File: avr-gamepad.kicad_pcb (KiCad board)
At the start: 2 copper layers, 26.7 x 48.3 mm, 33 parts, among them J1 Conn_01x08, J2 Conn_01x01, P1 USB_C_Plug_USB2.0, SW10 Up, SW11 Down, SW12 Left, SW13 Select, SW2 R, SW3 X, SW4 A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

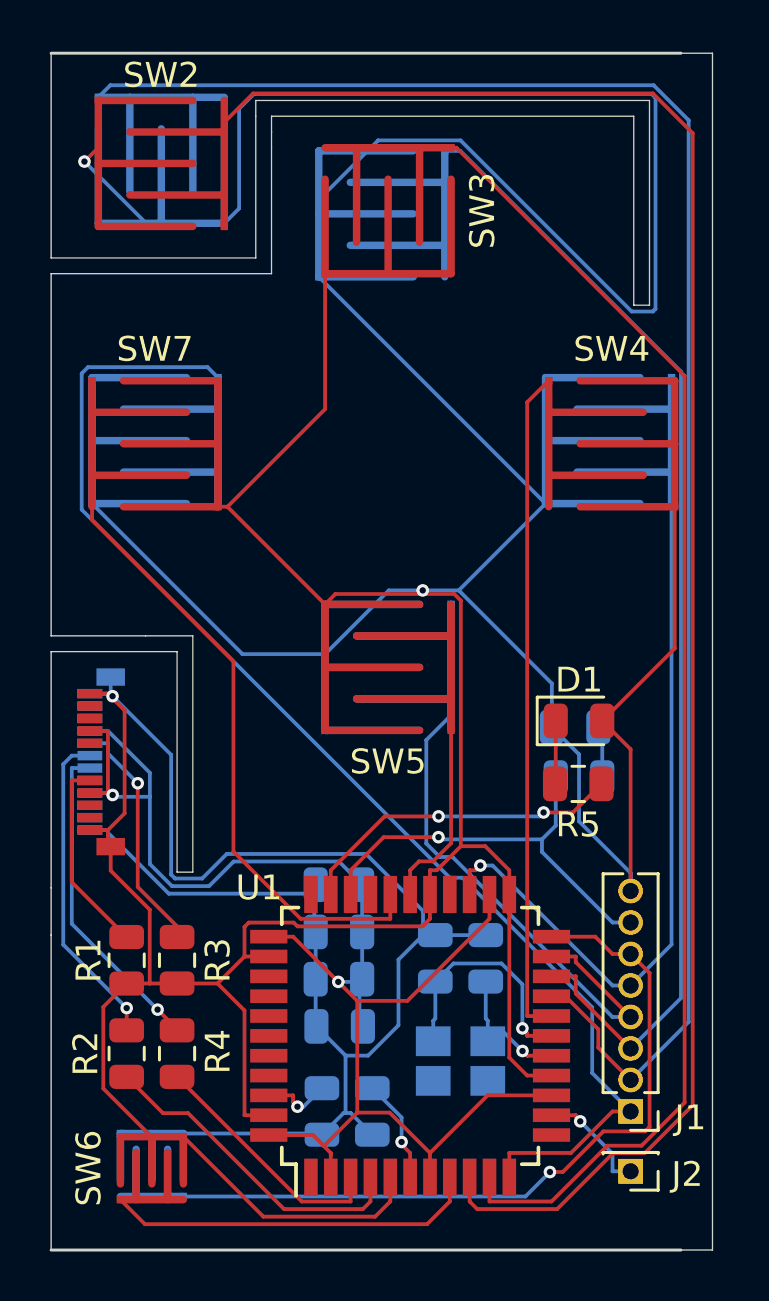
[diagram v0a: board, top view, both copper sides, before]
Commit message: tweak pcb outline for usb connector. Update gitignore
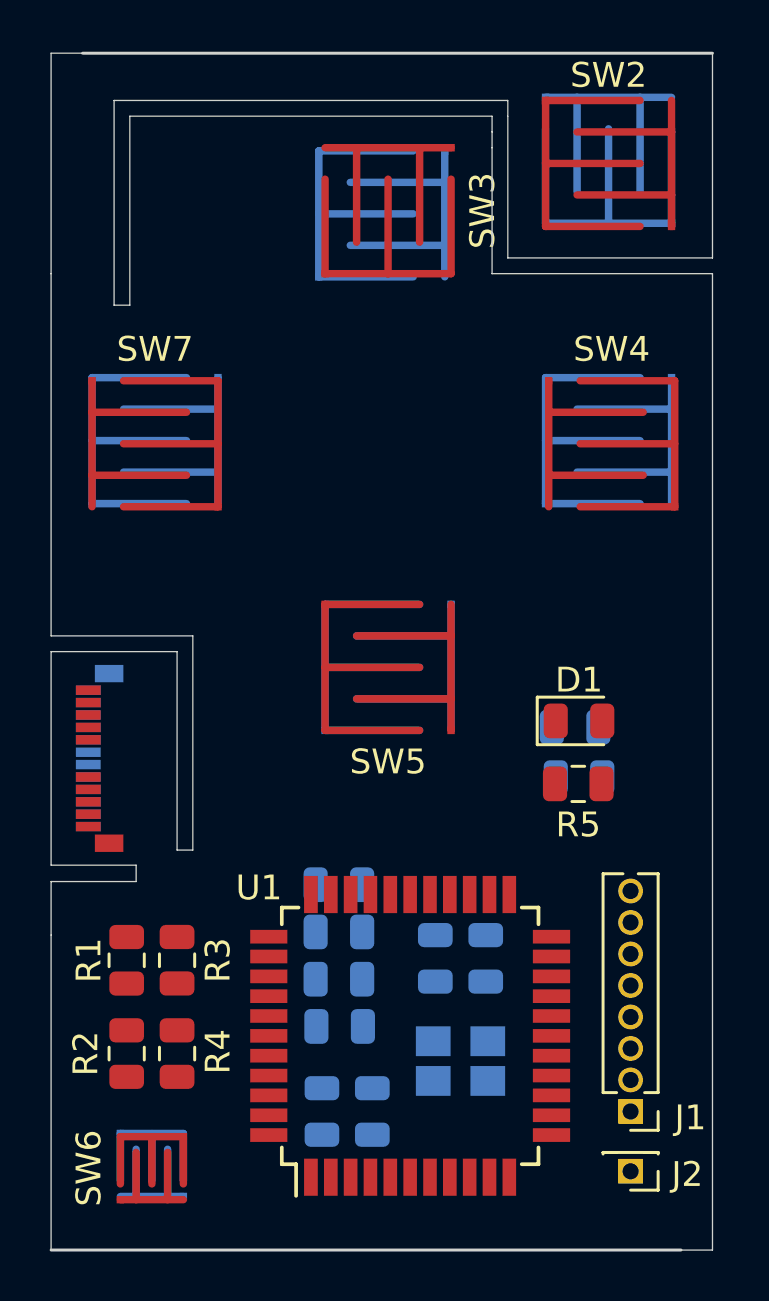
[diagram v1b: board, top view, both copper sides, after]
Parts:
- moved SW2 18.0 mm to (149.5, 83.2)
- moved SW9 18.0 mm to (149.5, 83.1)
- moved P1 0.15 mm to (128.5, 107.2)
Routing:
- net GND: track 298.5 -> 0.00 mm, vias 3 -> 0
- net /pb1: track 75.3 -> 0.00 mm
- net /pd1: track 69.3 -> 0.00 mm
- net +5V: track 62.8 -> 0.00 mm, vias 2 -> 0
- net /pb2: track 53.0 -> 0.00 mm
- net /pb3: track 51.6 -> 0.00 mm
- net /pd2: track 46.1 -> 0.00 mm
- net /pd4: track 34.7 -> 0.00 mm, vias 1 -> 0
- net /pd5: track 30.7 -> 0.00 mm, vias 1 -> 0
- net /pb5: track 29.8 -> 0.00 mm
- net /pd0: track 27.0 -> 0.00 mm
- net /pd3: track 25.5 -> 0.00 mm
- net /pc6: track 17.3 -> 0.00 mm, vias 1 -> 0
- net /pb0: track 15.1 -> 0.00 mm
- net /pc7: track 13.3 -> 0.00 mm, vias 2 -> 0
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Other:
- outline, holes or cut-outs redrawn

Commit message: pcb alignment hole, tweak CC resistor positions and start-select pads
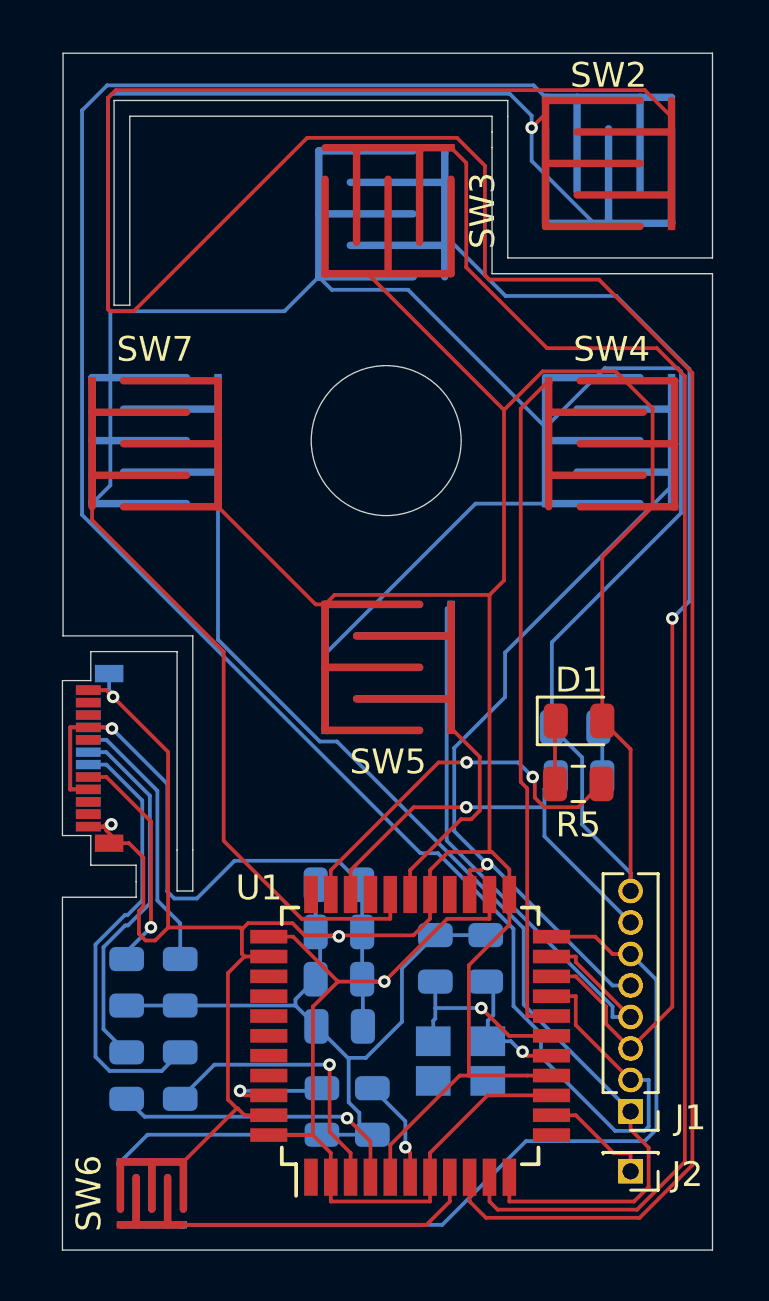
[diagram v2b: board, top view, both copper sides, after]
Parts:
- R1, R2, R3, R4: moved to B.Cu
- moved SW13 1.14 mm to (131.1, 124.7)
- moved SW6 1.02 mm to (131.1, 124.7)
- moved R3 0.90 mm to (132.2, 116.2)
- moved R4 0.90 mm to (132.2, 120.0)
- moved R1 0.89 mm to (130.0, 116.2)
- moved R2 0.89 mm to (130.0, 120.0)
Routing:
- net GND: track 0.00 -> 291.5 mm, vias 0 -> 4
- net /pb1: track 0.00 -> 112.3 mm
- net /pd1: track 0.00 -> 79.1 mm
- net +5V: track 0.00 -> 67.8 mm, vias 0 -> 2
- net /pb2: track 0.00 -> 57.2 mm
- net /pd2: track 0.00 -> 48.7 mm, vias 0 -> 1
- net /pb3: track 0.00 -> 47.1 mm
- net /pd4: track 0.00 -> 33.4 mm, vias 0 -> 1
- net /pd5: track 0.00 -> 31.7 mm
- net /pb5: track 0.00 -> 29.7 mm
- net /pd0: track 0.00 -> 27.2 mm
- net /pd3: track 0.00 -> 24.5 mm
- net Net-(P1-PadA7): track 0.00 -> 17.9 mm
- net /pc6: track 0.00 -> 17.3 mm, vias 0 -> 1
- net /pc7: track 0.00 -> 15.3 mm, vias 0 -> 2
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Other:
- board size 26.7 x 48.3 mm -> 26.2 x 48.3 mm

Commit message: replace headers with FFC connector. Adjust outline. Update gitignore
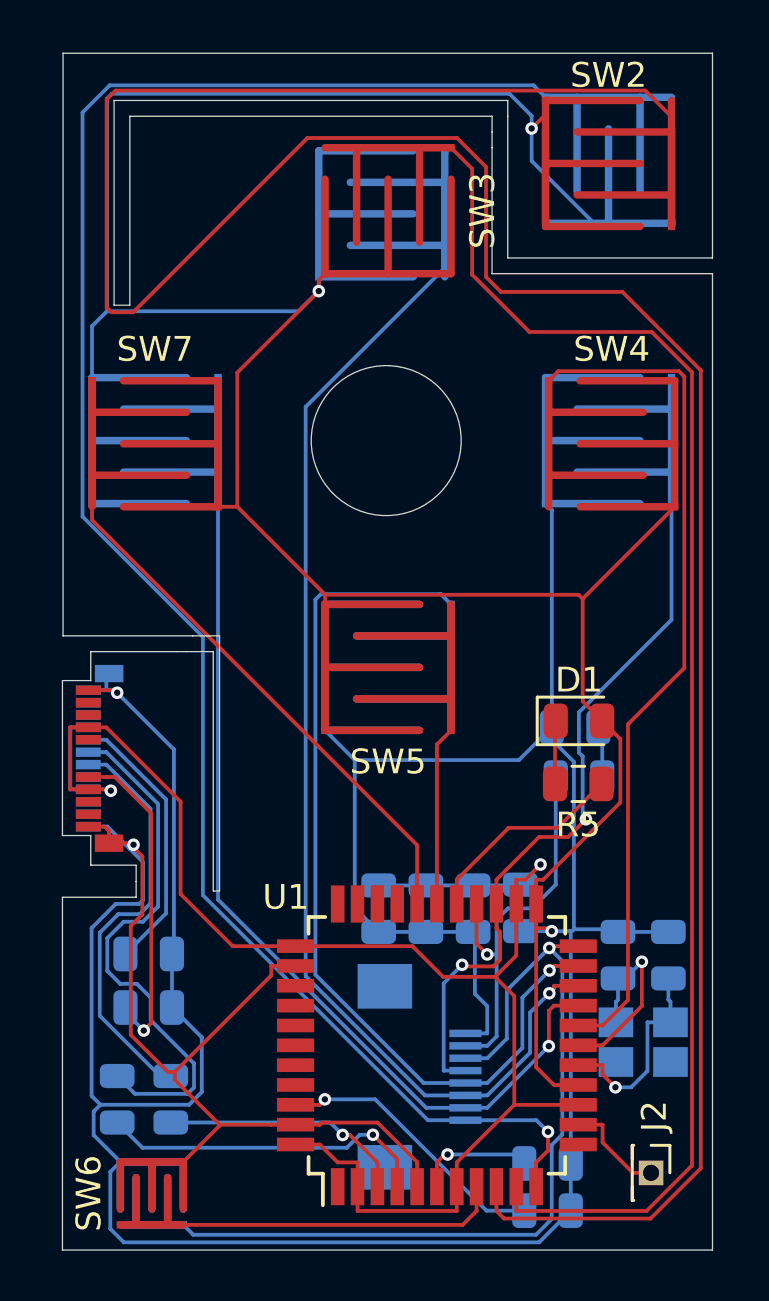
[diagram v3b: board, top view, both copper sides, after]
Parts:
- J1: footprint Connector_PinHeader_1.27mm:PinHeader_1x08_P1.27mm_Vertical -> Connector_FFC-FPC:Hirose_FH12-8S-0.5SH_1x08-1MP_P0.50mm_Horizontal; moved to B.Cu
- moved C7 9.94 mm to (147.0, 125.4), turned to 0 degrees
- moved C3 8.71 mm to (145.9, 113.2), turned to 270 degrees
- moved J1 8.62 mm to (141.9, 120.0), turned to 90 degrees
- moved Y1 7.41 mm to (150.9, 118.6)
- moved C8 7.37 mm to (147.0, 123.5), turned to 0 degrees
- moved C5 7.37 mm to (149.9, 115.1)
- moved C6 7.37 mm to (151.9, 115.1)
- moved C1 6.11 mm to (144.0, 113.2), turned to 270 degrees
- moved C2 3.63 mm to (142.1, 113.2), turned to 270 degrees
- moved C4 1.87 mm to (140.2, 113.2), turned to 270 degrees
- moved R3 1.71 mm to (130.9, 115.1), turned to 0 degrees
- moved R1 1.35 mm to (130.9, 117.2), turned to 0 degrees
- moved U1 1.15 mm to (142.6, 118.7)
- moved R2 1.03 mm to (129.7, 120.9)
- moved R4 1.03 mm to (131.8, 120.9)
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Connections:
- J1 pad 7: /pc6 -> /pd6
- R5 pad 2: /pc7 -> /pd7
- R6 pad 2: /pc6 -> /pd6
- SW8 pad 1: /pb3 -> /pd1
- SW9 pad 1: /pd1 -> /pb3
- U1 pad 27: GND -> /pd7
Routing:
- net /pd1: track 79.1 -> 41.6 mm, vias 0 -> 1
- net /pb3: track 47.1 -> 73.2 mm, vias 0 -> 1
- net GND: track 291.5 -> 270.1 mm, vias 4 -> 5
- net /pc6: track 17.3 -> 0.00 mm, vias 1 -> 0
- net /pd6: track 0.00 -> 16.0 mm, vias 0 -> 1
- net /pc7: track 15.3 -> 0.00 mm, vias 2 -> 0
- net /pd3: track 24.5 -> 36.4 mm, vias 0 -> 1
- net /pd7: track 0.00 -> 8.42 mm
- net /pd0: track 27.2 -> 34.2 mm
- net Net-(P1-PadA6): track 14.8 -> 21.8 mm
- net Net-(C7-Pad1): track 4.58 -> 11.2 mm
- net Net-(P1-PadB5): track 9.22 -> 13.3 mm
- net /pb5: track 29.7 -> 26.5 mm
- net Net-(C6-Pad1): track 5.43 -> 8.35 mm
- net /pd2: track 48.7 -> 51.4 mm
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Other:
- outline, holes or cut-outs redrawn

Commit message: pin reassignments
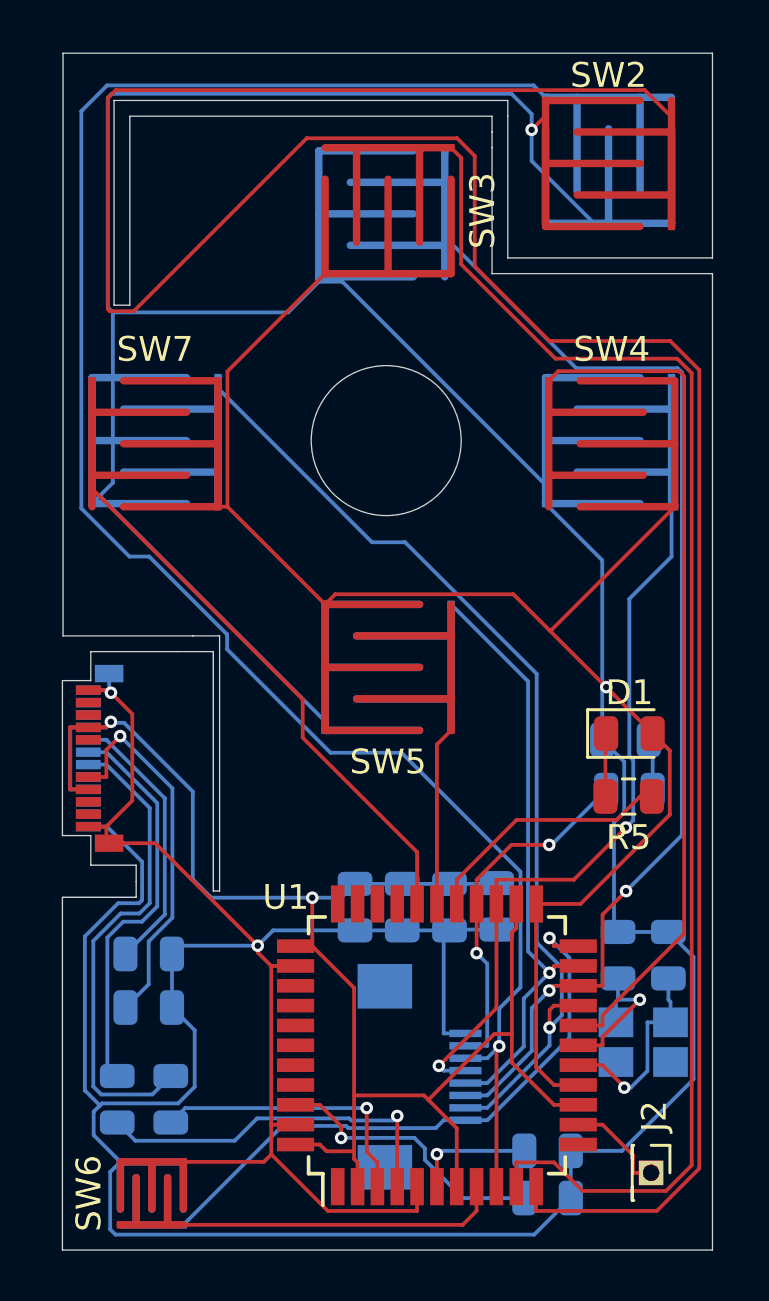
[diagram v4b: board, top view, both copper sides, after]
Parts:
- moved D2 2.09 mm to (150.2, 106.4)
- moved R5 2.09 mm to (150.3, 108.7)
- moved D1 2.09 mm to (150.3, 106.2)
- moved R6 2.09 mm to (150.3, 108.5)
- moved C2 0.96 mm to (141.2, 113.2)
- moved C3 0.96 mm to (145.0, 113.1)
- moved C1 0.95 mm to (143.1, 113.2)
- moved C4 0.95 mm to (139.3, 113.2)
- moved C7 0.51 mm to (147.0, 124.9)
- moved C8 0.51 mm to (147.0, 123.0)
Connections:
- J1 pad 1: /pb3 -> /pd5
- J1 pad 6: /pd5 -> /pb1
- SW2 pad 1: /pb1 -> /pb3
- SW9 pad 1: /pb3 -> /pb1
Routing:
- net /pb1: track 112.0 -> 74.2 mm, vias 0 -> 1
- net /pb3: track 73.2 -> 109.9 mm, vias 1 -> 0
- net /pd3: track 36.4 -> 24.2 mm
- net GND: track 270.1 -> 281.7 mm, vias 5 -> 4
- net /pd5: track 34.2 -> 24.5 mm
- net Net-(P1-PadA6): track 21.8 -> 16.1 mm
- net Net-(P1-PadA7): track 16.8 -> 19.4 mm
- net Net-(P1-PadB5): track 13.3 -> 15.2 mm
- net Net-(C5-Pad1): track 8.05 -> 6.13 mm
- net /pd7: track 8.42 -> 10.2 mm
- net /pd2: track 51.4 -> 49.7 mm, vias 1 -> 2
- net /pd1: track 41.6 -> 40.0 mm
- net /pd6: track 16.0 -> 14.5 mm, vias 1 -> 2
- net Net-(R4-Pad1): track 9.98 -> 11.5 mm
- net Net-(R2-Pad1): track 13.4 -> 14.9 mm
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
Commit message: trying and failing to autoroute with thicker power and ground traces
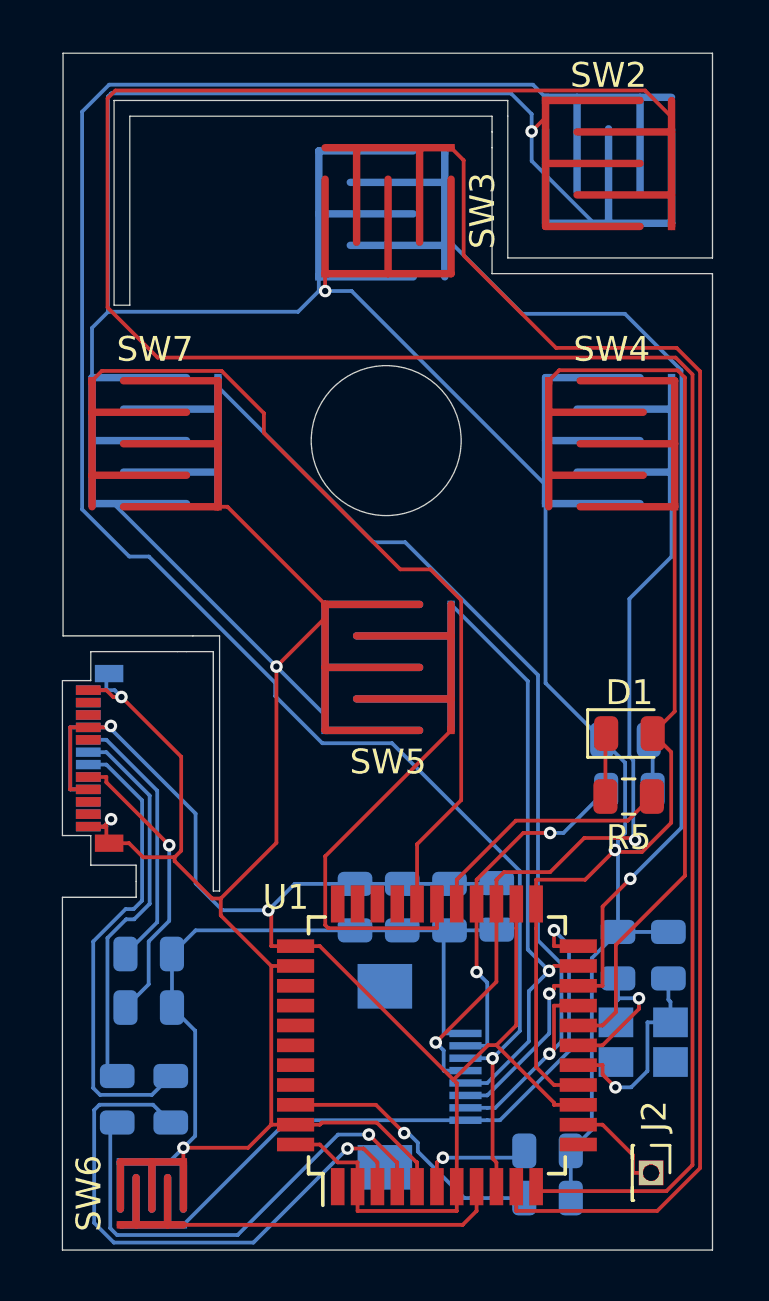
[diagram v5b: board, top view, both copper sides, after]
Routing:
- net GND: track 281.7 -> 234.9 mm, vias 4 -> 7
- net Net-(R4-Pad1): track 11.5 -> 22.6 mm
- net /pb3: track 109.9 -> 99.6 mm
- net /pb4: track 7.24 -> 15.5 mm
- net /pb5: track 26.5 -> 32.3 mm
- net Net-(R2-Pad1): track 14.9 -> 19.2 mm
- net Net-(P1-PadB5): track 15.2 -> 11.8 mm
- net /pd1: track 40.0 -> 41.2 mm
- net /pd4: track 34.7 -> 35.5 mm
- net +5V: track 67.7 -> 68.4 mm
- net /pd5: track 24.5 -> 25.2 mm
- net Net-(P1-PadA6): track 16.1 -> 15.6 mm

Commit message: move FFC connector and increase power and ground track width
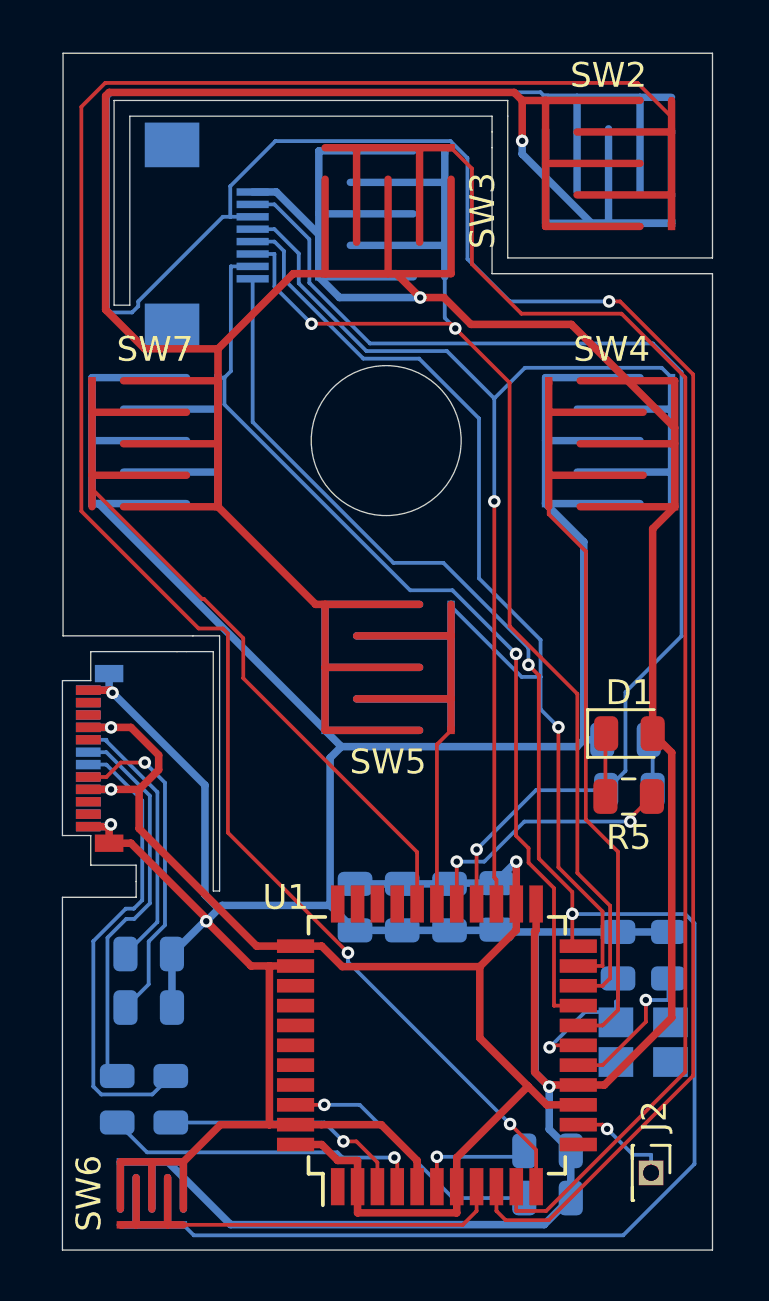
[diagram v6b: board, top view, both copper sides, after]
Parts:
- moved J1 35.0 mm to (133.3, 86.1)
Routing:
- net /pd5: track 25.2 -> 70.3 mm, vias 1 -> 2
- net /pd6: track 14.5 -> 47.7 mm, vias 2 -> 1
- net GND: track 234.9 -> 262.8 mm, vias 7 -> 6
- net /pb1: track 73.7 -> 100.7 mm
- net /pb3: track 99.6 -> 80.9 mm, vias 0 -> 2
- net /pd3: track 24.1 -> 42.7 mm
- net Net-(R4-Pad1): track 22.6 -> 9.98 mm
- net /pb4: track 15.5 -> 7.24 mm
- net +5V: track 68.4 -> 61.4 mm, vias 2 -> 3
- net Net-(R2-Pad1): track 19.2 -> 13.0 mm
- net /pd4: track 35.5 -> 41.5 mm, vias 2 -> 1
- net /pd0: track 34.3 -> 28.4 mm
- net /pb5: track 32.3 -> 26.6 mm
- net /pb2: track 57.3 -> 53.7 mm
- net /pd1: track 41.2 -> 38.5 mm
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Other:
- net class Power: trace_width 0.508 -> 0.3048
